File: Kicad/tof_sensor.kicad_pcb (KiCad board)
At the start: 2 copper layers, 86.4 x 45.7 mm, 52 parts, among them J1 Conn_01x06_Male, J2 Conn_01x05, Q1 BSH202,215, SW1 SW_DIP_x03, U1 MIC5504-2.8YM5, U2 PIC24FJ64GA002, U3 VL53L0X, U4 VL53L0X, U5 PCA9306

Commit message: Updated date on PCB
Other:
- board text added: "03/2020"
- board text removed: "12/2019"
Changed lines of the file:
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@@
     (effects (font (size 1 1) (thickness 0.15)) (justify mirror))
   )
-  (gr_text 12/2019 (at 158.75 104.14) (layer B.SilkS)
+  (gr_text 03/2020 (at 158.75 104.14) (layer B.SilkS)
     (effects (font (size 1 1) (thickness 0.15)) (justify mirror))
   )

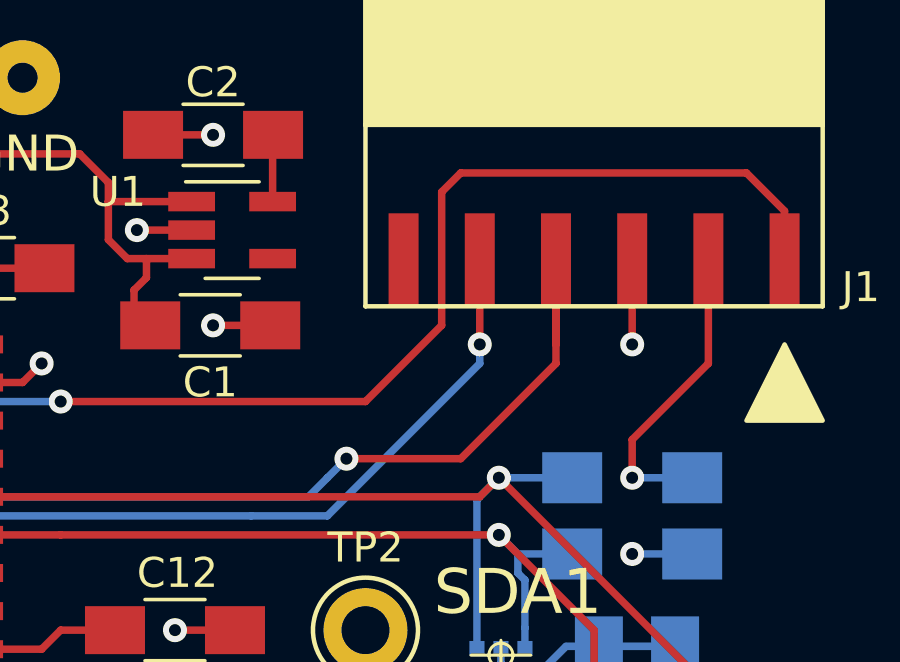
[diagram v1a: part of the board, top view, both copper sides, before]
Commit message: Changed net ICSP power pin
Changed from vdd to vcc, power now goes through the 2.8V LDO
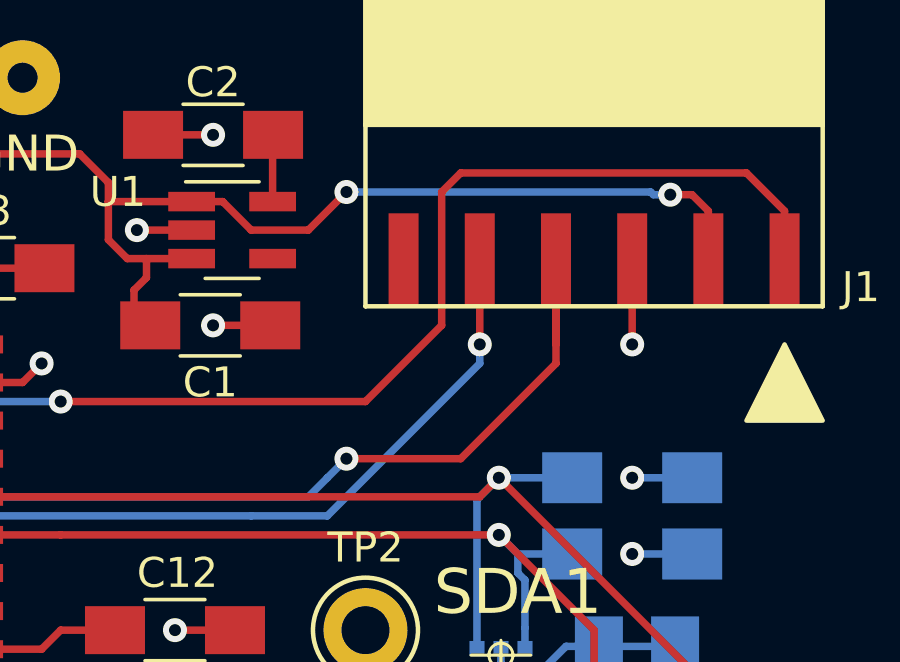
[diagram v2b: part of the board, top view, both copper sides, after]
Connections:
- J1 pad 2: VDD -> VCC
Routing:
- net VCC: track 65.8 -> 85.5 mm, vias 2 -> 4
- net VDD: track 51.3 -> 42.7 mm
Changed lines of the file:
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@@
     (thickness 1.6)
     (drawings 68)
-    (tracks 422)
+    (tracks 431)
     (zones 0)
     (modules 52)
@@
       (net 9 /ICSPCLK))
     (pad 2 smd rect (at 3.81 1.85 180) (size 1 3.1) (drill (offset 0 -0.3)) (layers F.Cu F.Paste F.Mask)
-      (net 3 VDD))
+      (net 1 VCC))
     (pad 3 smd rect (at 6.35 1.85 180) (size 1 3.1) (drill (offset 0 -0.3)) (layers F.Cu F.Paste F.Mask)
       (net 2 GND))
@@
   (segment (start 147.32 64.135) (end 149.86 66.675) (width 0.25) (layer F.Cu) (net 1))
   (segment (start 149.86 66.675) (end 164.465 66.675) (width 0.25) (layer F.Cu) (net 1))
+  (segment (start 185.42 69.905) (end 185.42 68.58) (width 0.25) (layer F.Cu) (net 1))
+  (via (at 184.15 68.035) (size 0.8) (drill 0.4) (layers F.Cu B.Cu) (net 1))
+  (segment (start 185.42 68.58) (end 184.875 68.035) (width 0.25) (layer F.Cu) (net 1))
+  (segment (start 184.875 68.035) (end 184.15 68.035) (width 0.25) (layer F.Cu) (net 1))
+  (segment (start 183.584315 68.035) (end 183.494315 67.945) (width 0.25) (layer B.Cu) (net 1))
+  (segment (start 184.15 68.035) (end 183.584315 68.035) (width 0.25) (layer B.Cu) (net 1))
+  (via (at 173.355 67.945) (size 0.8) (drill 0.4) (layers F.Cu B.Cu) (net 1))
+  (segment (start 183.494315 67.945) (end 173.355 67.945) (width 0.25) (layer B.Cu) (net 1))
+  (segment (start 169.23 68.265) (end 168.195 68.265) (width 0.25) (layer F.Cu) (net 1))
+  (segment (start 170.18 69.215) (end 169.23 68.265) (width 0.25) (layer F.Cu) (net 1))
+  (segment (start 173.355 67.945) (end 172.085 69.215) (width 0.25) (layer F.Cu) (net 1))
+  (segment (start 172.085 69.215) (end 170.18 69.215) (width 0.25) (layer F.Cu) (net 1))
   (via (at 133.35 80.645) (size 0.8) (drill 0.4) (layers F.Cu B.Cu) (net 2))
   (segment (start 133.35 80.645) (end 130.175 77.47) (width 0.25) (layer F.Cu) (net 2))
@@
   (segment (start 132.08 87.09) (end 132.08 85.09) (width 0.25) (layer B.Cu) (net 3))
   (via (at 132.08 85.09) (size 0.8) (drill 0.4) (layers F.Cu B.Cu) (net 3))
-  (segment (start 185.42 69.905) (end 185.42 73.66) (width 0.25) (layer F.Cu) (net 3))
-  (segment (start 182.88 76.2) (end 182.88 77.47) (width 0.25) (layer F.Cu) (net 3))
-  (segment (start 185.42 73.66) (end 182.88 76.2) (width 0.25) (layer F.Cu) (net 3))
   (segment (start 126.785 69.525) (end 126.365 69.945) (width 0.25) (layer F.Cu) (net 3))
   (segment (start 129.11 69.525) (end 126.785 69.525) (width 0.25) (layer F.Cu) (net 3))
